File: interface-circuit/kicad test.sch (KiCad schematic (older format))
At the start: 17 parts, among them J1 PumpSSR, J2 Probe, J3 GPIO, J4 Buzzer, J5 CoilSwitch, J6 FanPWR, J7 Rpi PWR, J8 ScreenPWR, J9 ATX PWR IN, Q1 2N3904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

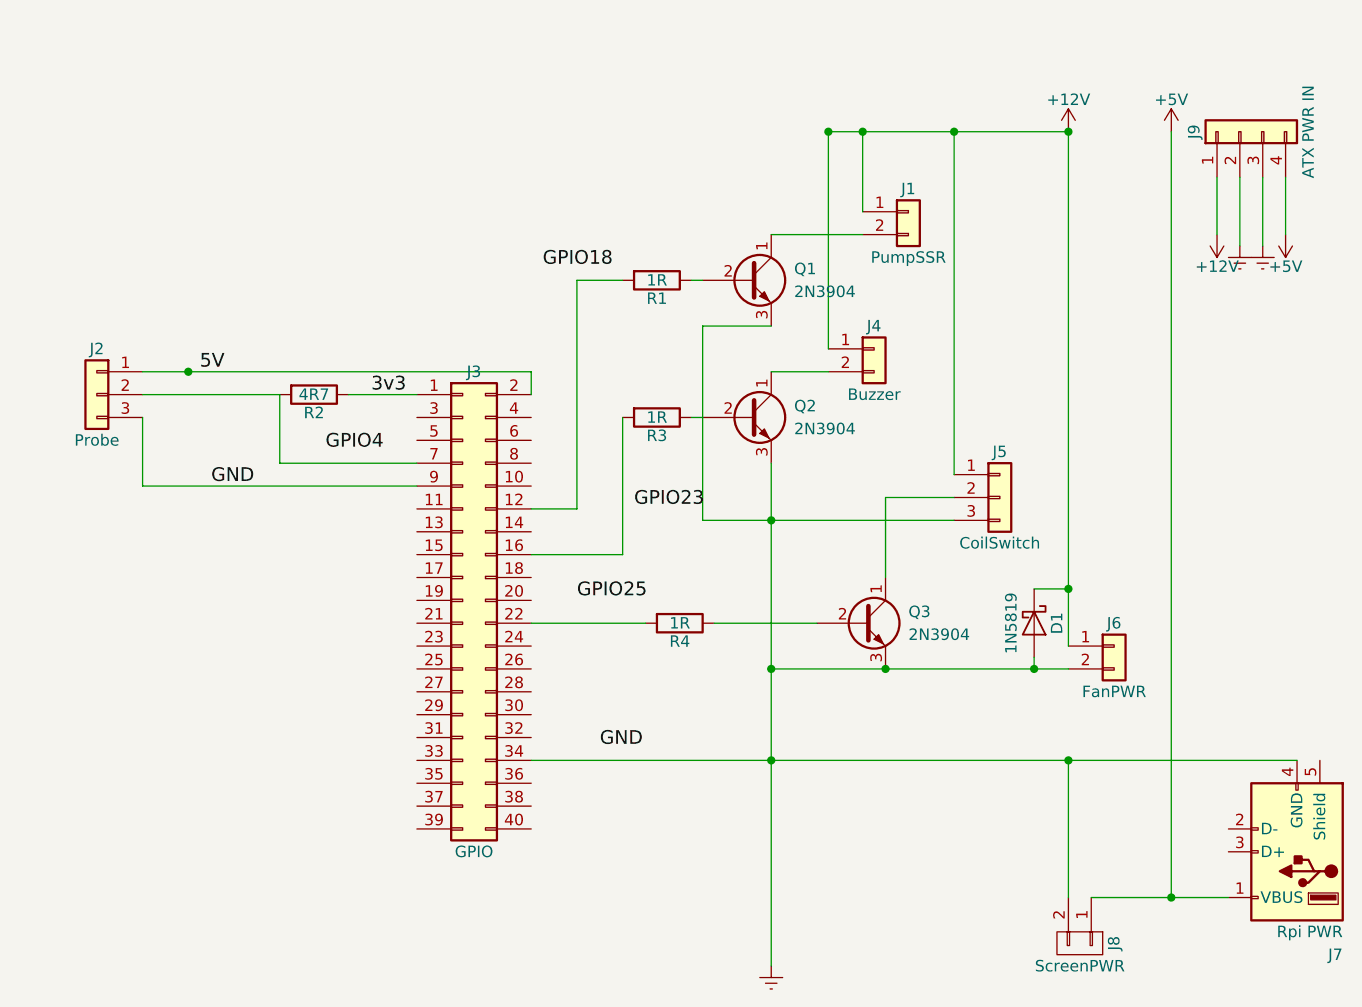
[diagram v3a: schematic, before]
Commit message: Add transistor control of fan, make pins match 3rd party board, switch to screw terminals
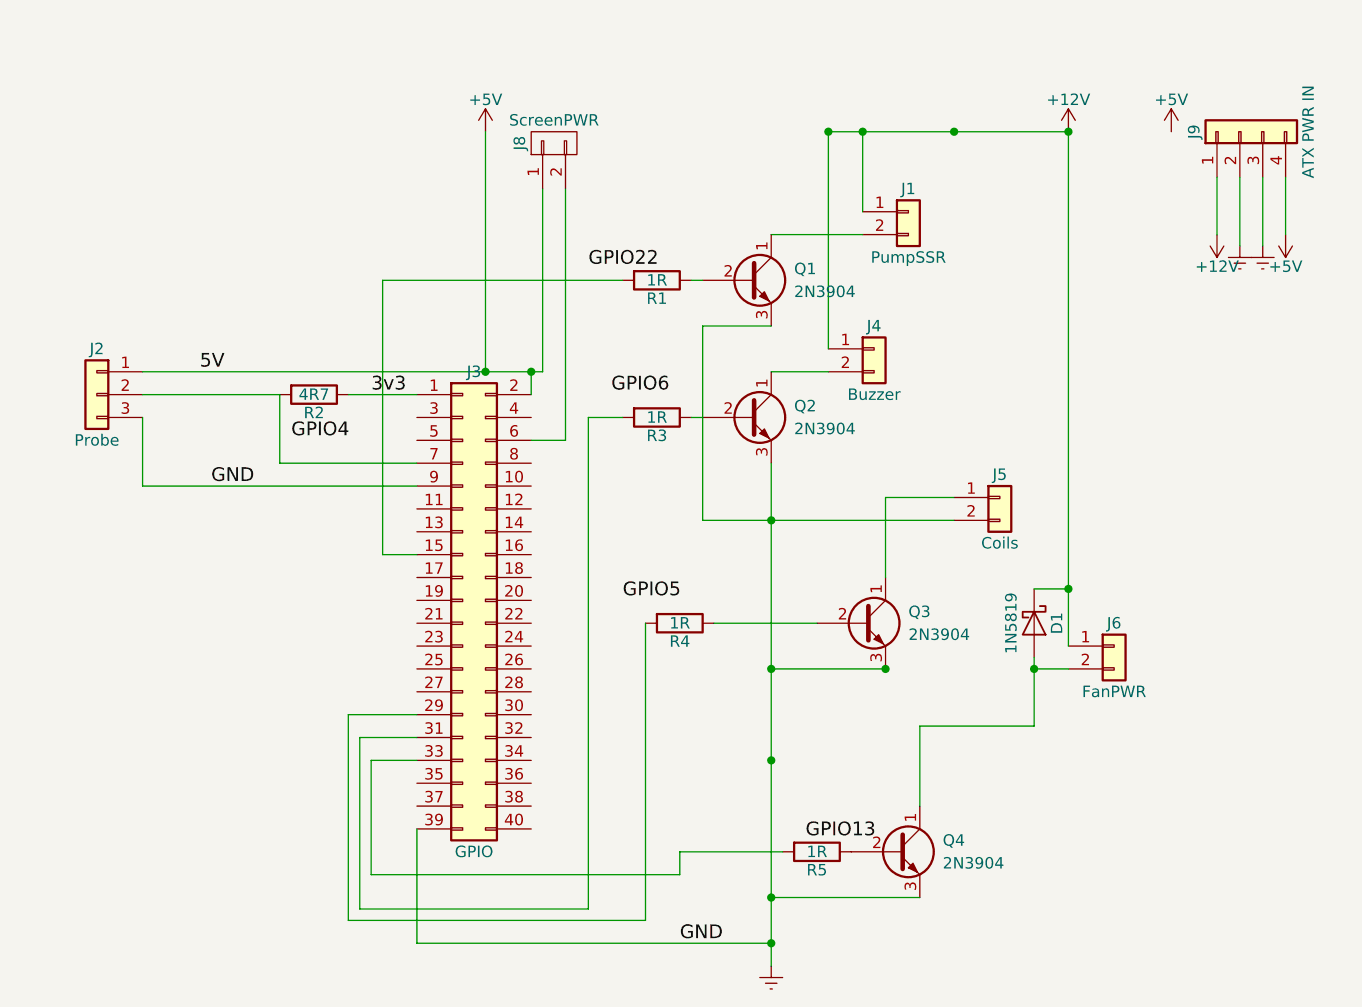
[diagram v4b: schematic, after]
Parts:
- removed J5: CoilSwitch, Connectors_JST:JST_XH_B03B-XH-A_03x2.50mm_Straight, symbol Conn_01x03
- removed J7: Rpi PWR, Connectors:USB_A, symbol USB_A
- added J5: Coils, Connectors_Terminal_Blocks:TerminalBlock_bornier-2_P5.08mm, symbol Conn_01x02
- added Q4: 2N3904, TO_SOT_Packages_THT:TO-92_Inline_Narrow_Oval, symbol Q_NPN_CBE
- added R5: 1R, Resistors_THT:R_Axial_DIN0309_L9.0mm_D3.2mm_P15.24mm_Horizontal, symbol R
- J1, J4: footprint Connectors_JST:JST_XH_B02B-XH-A_02x2.50mm_Straight -> Connectors_Terminal_Blocks:TerminalBlock_bornier-2_P5.08mm
- J2: footprint Pin_Headers:Pin_Header_Straight_1x03_Pitch2.54mm -> Connectors_Terminal_Blocks:TerminalBlock_bornier-3_P5.08mm
- J6: footprint Pin_Headers:Pin_Header_Straight_1x02_Pitch2.54mm -> Connectors_Terminal_Blocks:TerminalBlock_bornier-2_P5.08mm
- J8: footprint Pin_Headers:Pin_Header_Straight_1x02_Pitch2.54mm_SMD_Pin1Right -> Connectors_Terminal_Blocks:TerminalBlock_bornier-2_P5.08mm
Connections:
- net 5V is gone; now on net +5V: J2.1 (Pin_1), J3.2 (Pin_2)
- net GND is gone; now on net Earth: J2.3 (Pin_3), J3.9 (Pin_9)
- net Earth: now also J3.39 (Pin_39), J5.2 (Pin_2), Q4.3 (E); no longer D1.2 (A), J3.34 (Pin_34), J6.2 (Pin_2), J8.2 (P2)
- net at J3.12 (Pin_12): no longer R1.2
- net at J3.15 (Pin_15): now also R1.2
- net at J3.16 (Pin_16): no longer R3.2
- net at J3.22 (Pin_22): no longer R4.2
- net at J3.29 (Pin_29): now also R4.2
- net at J3.31 (Pin_31): now also R3.2
- net at J3.33 (Pin_33): now also R5.2
- net at J3.6 (Pin_6): now also J8.2 (P2)
- net at Q3.1 (C): now also J5.1 (Pin_1)
- new net: D1.2 (A), J6.2 (Pin_2), Q4.1 (C)
- new net: Q4.2 (B), R5.1
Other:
- moved on the sheet: J8
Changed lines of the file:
@@
-$EndComp
-$Comp
-L USB_A J7
-U 1 1 5A8BF5B4
-P 10000 4600
-F 0 "J7" H 9800 5050 50  0000 L CNN
-F 1 "Rpi PWR" H 9800 4950 50  0000 L CNN
-F 2 "Connectors:USB_A" H 10150 4550 50  0001 C CNN
-F 3 "" H 10150 4550 50  0001 C CNN
-	1    10000 4600
-	-1   0    0    1
 $EndComp
 $Comp
@@
 F 0 "J4" H 8150 2500 50  0000 C CNN
 F 1 "Buzzer" H 8150 2200 50  0000 C CNN
-F 2 "Connectors_JST:JST_XH_B02B-XH-A_02x2.50mm_Straight" H 8150 2400 50  0001 C CNN
+F 2 "Connectors_Terminal_Blocks:TerminalBlock_bornier-2_P5.08mm" H 8150 2400 50  0001 C CNN
 F 3 "" H 8150 2400 50  0001 C CNN
 	1    8150 2400
@@
 F 0 "J1" H 8300 1900 50  0000 C CNN
 F 1 "PumpSSR" H 8300 1600 50  0000 C CNN
-F 2 "Connectors_JST:JST_XH_B02B-XH-A_02x2.50mm_Straight" H 8300 1800 50  0001 C CNN
+F 2 "Connectors_Terminal_Blocks:TerminalBlock_bornier-2_P5.08mm" H 8300 1800 50  0001 C CNN
 F 3 "" H 8300 1800 50  0001 C CNN
 	1    8300 1800
@@
 F 0 "J6" H 9200 3800 50  0000 C CNN
 F 1 "FanPWR" H 9200 3500 50  0000 C CNN
-F 2 "Pin_Headers:Pin_Header_Straight_1x02_Pitch2.54mm" H 9200 3700 50  0001 C CNN
+F 2 "Connectors_Terminal_Blocks:TerminalBlock_bornier-2_P5.08mm" H 9200 3700 50  0001 C CNN
 F 3 "" H 9200 3700 50  0001 C CNN
 	1    9200 3700
@@
 F 0 "J2" H 4750 2800 50  0000 C CNN
 F 1 "Probe" H 4750 2400 50  0000 C CNN
-F 2 "Pin_Headers:Pin_Header_Straight_1x03_Pitch2.54mm" H 4750 2600 50  0001 C CNN
+F 2 "Connectors_Terminal_Blocks:TerminalBlock_bornier-3_P5.08mm" H 4750 2600 50  0001 C CNN
 F 3 "" H 4750 2600 50  0001 C CNN
 	1    4750 2600
 	-1   0    0    -1
-$EndComp
-$Comp
-L Conn_01x03 J5
-U 1 1 5A8CC827
-P 8700 3050
-F 0 "J5" H 8700 3250 50  0000 C CNN
-F 1 "CoilSwitch" H 8700 2850 50  0000 C CNN
-F 2 "Connectors_JST:JST_XH_B03B-XH-A_03x2.50mm_Straight" H 8700 3050 50  0001 C CNN
-F 3 "" H 8700 3050 50  0001 C CNN
-	1    8700 3050
-	1    0    0    -1
 $EndComp
 $Comp
@@
 Wire Wire Line
 	7700 2900 7700 5100
-Wire Wire Line
-	6650 3300 7050 3300
-Wire Wire Line
-	7050 3300 7050 2700
-Text Label 7100 3100 0    60   ~ 0
-GPIO23
+Text Label 7000 2600 0    60   ~ 0
+GPIO6
 Wire Wire Line
 	7950 2400 7950 1450
 Wire Wire Line
 	7950 1450 9000 1450
-Text Label 6850 3500 0    60   ~ 0
-GPIO25
-Wire Wire Line
-	6650 3600 7150 3600
+Text Label 7050 3500 0    60   ~ 0
+GPIO5
 Wire Wire Line
 	7450 3600 7900 3600
-Wire Wire Line
-	8500 2950 8500 1450
 Connection ~ 8500 1450
 Wire Wire Line
@@
 Connection ~ 9000 1450
 Wire Wire Line
-	7700 3800 9000 3800
+	7700 3800 8200 3800
+Wire Wire Line
+	8850 3800 9000 3800
 Connection ~ 7700 3800
 Wire Wire Line
-	8850 3750 8850 3800
+	8850 3750 8850 4050
 Connection ~ 8850 3800
 Wire Wire Line
 	8850 3450 9000 3450
 Connection ~ 9000 3450
-Wire Wire Line
-	6650 4200 10000 4200
 Connection ~ 7700 4200
-Text Label 6950 4150 0    60   ~ 0
+Text Label 7300 5000 0    60   ~ 0
 GND
 Wire Wire Line
@@
 Wire Wire Line
 	5550 2900 6150 2900
-Text Label 5750 2850 0    60   ~ 0
+Text Label 5600 2800 0    60   ~ 0
 GPIO4
 Wire Wire Line
 	6650 2500 6650 2600
-Wire Wire Line
-	4950 2500 6650 2500
 Text Label 5200 2500 0    60   ~ 0
 5V
@@
 Text Label 5250 3000 0    60   ~ 0
 GND
-Wire Wire Line
-	8200 3800 8200 3800
 Connection ~ 8200 3800
 Connection ~ 7950 1450
-Wire Wire Line
-	6650 3100 6850 3100
-Wire Wire Line
-	6850 3100 6850 2100
-Wire Wire Line
-	6850 2100 7050 2100
-Text Label 6700 2050 0    60   ~ 0
-GPIO18
+Text Label 6900 2050 0    60   ~ 0
+GPIO22
 Wire Wire Line
 	7350 2100 7400 2100
@@
 Wire Wire Line
 	7400 2300 7400 3150
-Wire Wire Line
-	9100 4800 9700 4800
 Wire Wire Line
 	7950 2500 7700 2500
@@
 	9850 1650 9850 1950
 Wire Wire Line
-	9450 1450 9450 4800
-Connection ~ 5150 2500
-Wire Wire Line
 	4950 3000 6150 3000
 $Comp
 L CONN_01X02 J8
 U 1 1 5A9D33AF
-P 9050 5000
-F 0 "J8" H 9050 5150 50  0000 C CNN
-F 1 "ScreenPWR" V 9150 5000 50  0000 C CNN
-F 2 "Pin_Headers:Pin_Header_Straight_1x02_Pitch2.54mm_SMD_Pin1Right" H 9050 5000 50  0001 C CNN
-F 3 "" H 9050 5000 50  0001 C CNN
-	1    9050 5000
+P 6750 1500
+F 0 "J8" H 6750 1650 50  0000 C CNN
+F 1 "ScreenPWR" V 6850 1500 50  0000 C CNN
+F 2 "Connectors_Terminal_Blocks:TerminalBlock_bornier-2_P5.08mm" H 6750 1500 50  0001 C CNN
+F 3 "" H 6750 1500 50  0001 C CNN
+	1    6750 1500
+	0    -1   -1   0
+$EndComp
+Wire Wire Line
+	5850 4900 7150 4900
+Wire Wire Line
+	7150 4900 7150 3600
+$Comp
+L Q_NPN_CBE Q4
+U 1 1 5B480BC7
+P 8250 4600
+F 0 "Q4" H 8450 4650 50  0000 L CNN
+F 1 "2N3904" H 8450 4550 50  0000 L CNN
+F 2 "TO_SOT_Packages_THT:TO-92_Inline_Narrow_Oval" H 8450 4700 50  0001 C CNN
+F 3 "" H 8250 4600 50  0001 C CNN
+	1    8250 4600
+	1    0    0    -1
+$EndComp
+Wire Wire Line
+	8850 4050 8350 4050
+Wire Wire Line
+	8350 4050 8350 4400
+Wire Wire Line
+	8350 4800 7700 4800
+Connection ~ 7700 4800
+$Comp
+L R R5
+U 1 1 5B480F66
+P 7900 4600
+F 0 "R5" V 7980 4600 50  0000 C CNN
+F 1 "1R" V 7900 4600 50  0000 C CNN
+F 2 "Resistors_THT:R_Axial_DIN0309_L9.0mm_D3.2mm_P15.24mm_Horizontal" V 7830 4600 50  0001 C CNN
+F 3 "" H 7900 4600 50  0001 C CNN
+	1    7900 4600
 	0    1    1    0
 $EndComp
-Connection ~ 9450 4800
-Wire Wire Line
-	9000 4800 9000 4200
-Connection ~ 9000 4200
+Wire Wire Line
+	7750 4600 7300 4600
+Wire Wire Line
+	7300 4600 7300 4700
+Wire Wire Line
+	7300 4700 5950 4700
+Wire Wire Line
+	4950 2500 6700 2500
+$Comp
+L +5V #PWR08
+U 1 1 5B4819C6
+P 6450 1450
+F 0 "#PWR08" H 6450 1300 50  0001 C CNN
+F 1 "+5V" H 6450 1590 50  0000 C CNN
+F 2 "" H 6450 1450 50  0001 C CNN
+F 3 "" H 6450 1450 50  0001 C CNN
+	1    6450 1450
+	1    0    0    -1
+$EndComp
+Wire Wire Line
+	6450 1450 6450 2500
+Connection ~ 6450 2500
+Wire Wire Line
+	6700 2500 6700 1700
+Connection ~ 6650 2500
+Text Label 7850 4550 0    60   ~ 0
+GPIO13
+Wire Wire Line
+	6650 2800 6800 2800
+Wire Wire Line
+	6800 2800 6800 1700
+Wire Wire Line
+	6150 3300 6000 3300
+Wire Wire Line
+	6000 3300 6000 2100
+Wire Wire Line
+	6000 2100 7050 2100
+Wire Wire Line
+	6150 4000 5850 4000
+Wire Wire Line
+	5850 4000 5850 4900
+Wire Wire Line
+	7050 2700 6900 2700
+Wire Wire Line
+	6900 2700 6900 4850
+Wire Wire Line
+	6150 4100 5900 4100
+Wire Wire Line
+	5900 4100 5900 4850
+Wire Wire Line
+	5900 4850 6900 4850
+Wire Wire Line
+	6150 4200 5950 4200
+Wire Wire Line
+	5950 4200 5950 4700
+$Comp
+L Conn_01x02 J5
+U 1 1 5B4837E7
+P 8700 3050
+F 0 "J5" H 8700 3150 50  0000 C CNN
+F 1 "Coils" H 8700 2850 50  0000 C CNN
+F 2 "Connectors_Terminal_Blocks:TerminalBlock_bornier-2_P5.08mm" H 8700 3050 50  0001 C CNN
+F 3 "" H 8700 3050 50  0001 C CNN
+	1    8700 3050
+	1    0    0    -1
+$EndComp
+Wire Wire Line
+	6150 4500 6150 5000
+Wire Wire Line
+	6150 5000 7700 5000
+Connection ~ 7700 5000
 $EndSCHEMATC

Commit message: New PCB layout using only screw terminals
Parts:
- removed J9: ATX PWR IN, Connectors_Phoenix:PhoenixContact_MSTBVA-G_04x5.08mm_Vertical, symbol Conn_01x04
- added J9: Screw_Terminal_01x03, Connectors_Terminal_Blocks:TerminalBlock_bornier-3_P5.08mm, symbol Screw_Terminal_01x03
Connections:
- net +12V: now also J9.1 (Pin_1)
- net +5V: now also J9.3 (Pin_3)
- net Earth: now also J8.2 (P2), J9.2 (Pin_2); no longer J3.39 (Pin_39)
- net at J3.6 (Pin_6): no longer J8.2 (P2)
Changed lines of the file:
@@
 $EndComp
 $Comp
-L +5V #PWR02
-U 1 1 5A8CCC1C
-P 9450 1450
-F 0 "#PWR02" H 9450 1300 50  0001 C CNN
-F 1 "+5V" H 9450 1590 50  0000 C CNN
-F 2 "" H 9450 1450 50  0001 C CNN
-F 3 "" H 9450 1450 50  0001 C CNN
-	1    9450 1450
-	1    0    0    -1
-$EndComp
-$Comp
-L Earth #PWR03
+L Earth #PWR02
 U 1 1 5A8CCC6C
 P 7700 5100
-F 0 "#PWR03" H 7700 4850 50  0001 C CNN
+F 0 "#PWR02" H 7700 4850 50  0001 C CNN
 F 1 "Earth" H 7700 4950 50  0001 C CNN
 F 2 "" H 7700 5100 50  0001 C CNN
@@
 	7950 2500 7700 2500
 $Comp
-L Conn_01x04 J9
-U 1 1 5A8E615F
-P 9750 1450
-F 0 "J9" H 9750 1650 50  0000 C CNN
-F 1 "ATX PWR IN" H 9750 1150 50  0000 C CNN
-F 2 "Connectors_Phoenix:PhoenixContact_MSTBVA-G_04x5.08mm_Vertical" H 9750 1450 50  0001 C CNN
-F 3 "" H 9750 1450 50  0001 C CNN
-	1    9750 1450
-	0    -1   -1   0
-$EndComp
-$Comp
-L +12V #PWR04
+L +12V #PWR03
 U 1 1 5A8E6215
 P 9650 1900
-F 0 "#PWR04" H 9650 1750 50  0001 C CNN
+F 0 "#PWR03" H 9650 1750 50  0001 C CNN
 F 1 "+12V" H 9650 2040 50  0000 C CNN
 F 2 "" H 9650 1900 50  0001 C CNN
@@
 	9650 1650 9650 1900
 $Comp
-L +5V #PWR05
+L +5V #PWR04
 U 1 1 5A8E6304
-P 9950 1900
-F 0 "#PWR05" H 9950 1750 50  0001 C CNN
-F 1 "+5V" H 9950 2040 50  0000 C CNN
-F 2 "" H 9950 1900 50  0001 C CNN
-F 3 "" H 9950 1900 50  0001 C CNN
-	1    9950 1900
+P 10000 2200
+F 0 "#PWR04" H 10000 2050 50  0001 C CNN
+F 1 "+5V" H 10000 2340 50  0000 C CNN
+F 2 "" H 10000 2200 50  0001 C CNN
+F 3 "" H 10000 2200 50  0001 C CNN
+	1    10000 2200
 	-1   0    0    1
 $EndComp
-Wire Wire Line
-	9950 1900 9950 1650
-$Comp
-L Earth #PWR06
+$Comp
+L Earth #PWR05
 U 1 1 5A8E654C
 P 9750 1950
-F 0 "#PWR06" H 9750 1700 50  0001 C CNN
+F 0 "#PWR05" H 9750 1700 50  0001 C CNN
 F 1 "Earth" H 9750 1800 50  0001 C CNN
 F 2 "" H 9750 1950 50  0001 C CNN
@@
 	1    0    0    -1
 $EndComp
-$Comp
-L Earth #PWR07
-U 1 1 5A8E65A4
-P 9850 1950
-F 0 "#PWR07" H 9850 1700 50  0001 C CNN
-F 1 "Earth" H 9850 1800 50  0001 C CNN
-F 2 "" H 9850 1950 50  0001 C CNN
-F 3 "" H 9850 1950 50  0001 C CNN
-	1    9850 1950
-	1    0    0    -1
-$EndComp
 Wire Wire Line
 	9750 1650 9750 1950
-Wire Wire Line
-	9850 1650 9850 1950
 Wire Wire Line
 	4950 3000 6150 3000
@@
 	4950 2500 6700 2500
 $Comp
-L +5V #PWR08
+L +5V #PWR06
 U 1 1 5B4819C6
 P 6450 1450
-F 0 "#PWR08" H 6450 1300 50  0001 C CNN
+F 0 "#PWR06" H 6450 1300 50  0001 C CNN
 F 1 "+5V" H 6450 1590 50  0000 C CNN
 F 2 "" H 6450 1450 50  0001 C CNN
@@
 Text Label 7850 4550 0    60   ~ 0
 GPIO13
-Wire Wire Line
-	6650 2800 6800 2800
-Wire Wire Line
-	6800 2800 6800 1700
 Wire Wire Line
 	6150 3300 6000 3300
@@
 	1    0    0    -1
 $EndComp
-Wire Wire Line
-	6150 4500 6150 5000
-Wire Wire Line
-	6150 5000 7700 5000
 Connection ~ 7700 5000
+Wire Wire Line
+	9850 1650 9850 1950
+Wire Wire Line
+	9850 1950 9950 1950
+Wire Wire Line
+	9950 1950 9950 2200
+Wire Wire Line
+	9950 2200 10000 2200
+$Comp
+L Screw_Terminal_01x03 J9
+U 1 1 5B4B55B2
+P 9750 1450
+F 0 "J9" H 9750 1650 50  0000 C CNN
+F 1 "Screw_Terminal_01x03" H 9750 1250 50  0000 C CNN
+F 2 "Connectors_Terminal_Blocks:TerminalBlock_bornier-3_P5.08mm" H 9750 1450 50  0001 C CNN
+F 3 "" H 9750 1450 50  0001 C CNN
+	1    9750 1450
+	0    -1   -1   0
+$EndComp
+Wire Wire Line
+	6800 1700 5900 1700
+Wire Wire Line
+	5900 1700 5900 3000
+Connection ~ 5900 3000
+Wire Wire Line
+	7700 5000 5550 5000
+Wire Wire Line
+	5550 5000 5550 3000
+Connection ~ 5550 3000
 $EndSCHEMATC
